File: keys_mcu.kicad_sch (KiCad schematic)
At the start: 26 parts, among them J3 Conn_01x26_Socket, J5 Conn_ARM_JTAG_SWD_10, SW1 PWR, SW2 MUTE, SW2 Volume, SW3 PREV, SW4 PLAY_PAUSE, SW5 NEXT, U2 STM32G431CBUx

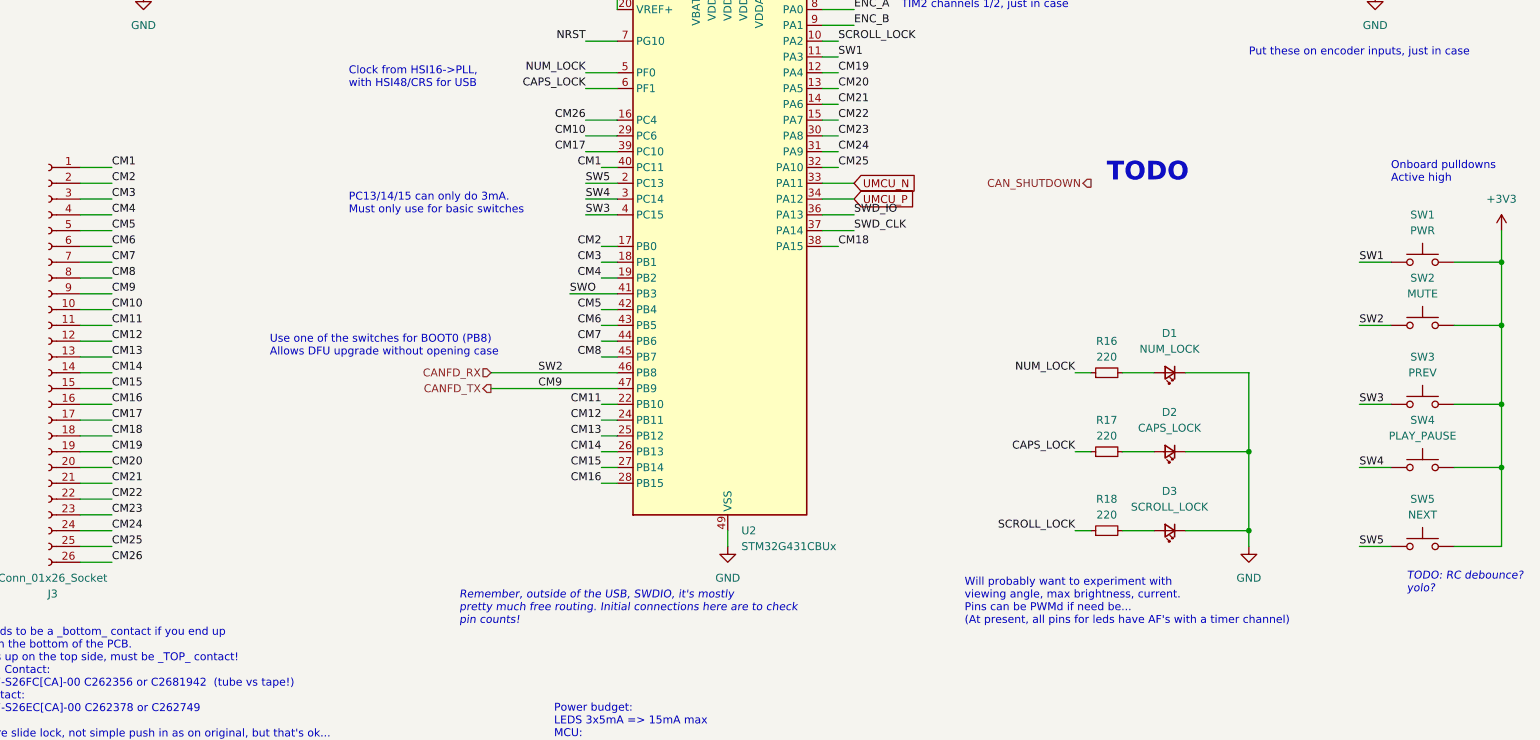
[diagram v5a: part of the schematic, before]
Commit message: unrouted: 0
Juggled all the key matrix IOs and reviewed "all" outstanding TODOs

left: add another cap for downstream Vbus.  it's free, and can only
help.

left: lots of silk?
left: place as much free io to pads as can be easily done, for
test/board reuse.
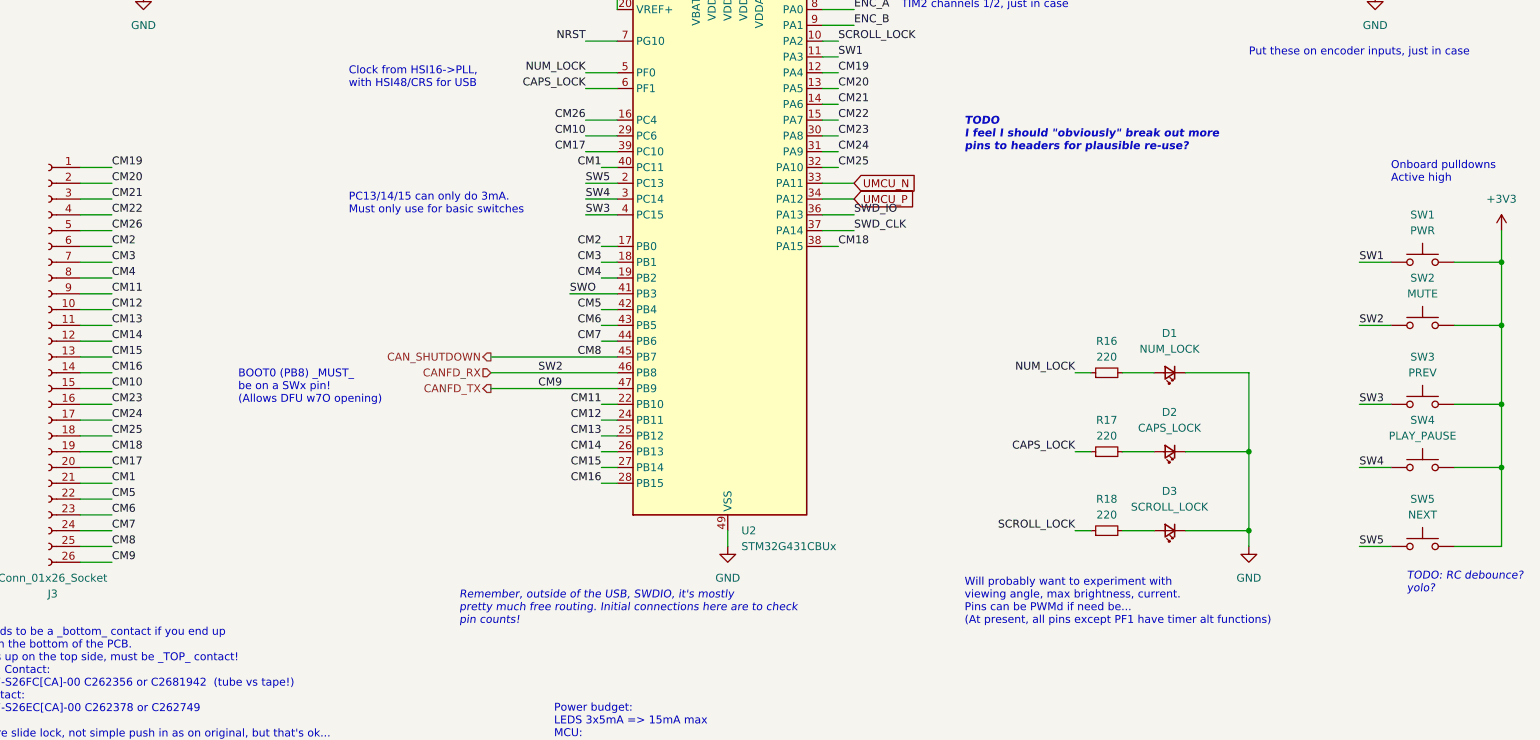
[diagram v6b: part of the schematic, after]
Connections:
- net CANFD_TX: now also J3.26 (Pin_26); no longer J3.9 (Pin_9)
- net CAN_SHUTDOWN: now also J3.25 (Pin_25), U2.45 (PB7)
- net CM1: now also J3.21 (Pin_21); no longer J3.1 (Pin_1)
- net CM10: now also J3.15 (Pin_15); no longer J3.10 (Pin_10)
- net CM11: now also J3.9 (Pin_9); no longer J3.11 (Pin_11)
- net CM12: now also J3.10 (Pin_10); no longer J3.12 (Pin_12)
- net CM13: now also J3.11 (Pin_11); no longer J3.13 (Pin_13)
- net CM14: now also J3.12 (Pin_12); no longer J3.14 (Pin_14)
- net CM15: now also J3.13 (Pin_13); no longer J3.15 (Pin_15)
- net CM16: now also J3.14 (Pin_14); no longer J3.16 (Pin_16)
- net CM17: now also J3.20 (Pin_20); no longer J3.17 (Pin_17)
- net CM18: now also J3.19 (Pin_19); no longer J3.18 (Pin_18)
- net CM19: now also J3.1 (Pin_1); no longer J3.19 (Pin_19)
- net CM2: now also J3.6 (Pin_6); no longer J3.2 (Pin_2)
- net CM20: now also J3.2 (Pin_2); no longer J3.20 (Pin_20)
- net CM21: now also J3.3 (Pin_3); no longer J3.21 (Pin_21)
- net CM22: now also J3.4 (Pin_4); no longer J3.22 (Pin_22)
- net CM23: now also J3.16 (Pin_16); no longer J3.23 (Pin_23)
- net CM24: now also J3.17 (Pin_17); no longer J3.24 (Pin_24)
- net CM25: now also J3.18 (Pin_18); no longer J3.25 (Pin_25)
- net CM26: now also J3.5 (Pin_5); no longer J3.26 (Pin_26)
- net CM3: now also J3.7 (Pin_7); no longer J3.3 (Pin_3)
- net CM4: now also J3.8 (Pin_8); no longer J3.4 (Pin_4)
- net CM5: now also J3.22 (Pin_22); no longer J3.5 (Pin_5)
- net CM6: now also J3.23 (Pin_23); no longer J3.6 (Pin_6)
- net CM7: now also J3.24 (Pin_24); no longer J3.7 (Pin_7)
- removed net CM8: J3.8 (Pin_8), U2.45 (PB7)
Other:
- note added: "BOOT0 (PB8) _MUST_ be on a SWx pin! (Allows DFU w7O opening)"
- note added: "TODO I feel I should "obviously" break out more pins to headers for plausible re-use?"
- note added: "Will probably want to experiment with viewing angle, max brightness, current. Pins can be PWMd if need be... (At present, all pins except PF1 have timer alt functions)"
- note removed: "TODO"
- note removed: "Use one of the switches for BOOT0 (PB8) Allows DFU upgrade without opening case"
- note removed: "Will probably want to experiment with viewing angle, max brightness, current. Pins can be PWMd if need be... (At present, all pins for leds have AF's with a timer channel)"
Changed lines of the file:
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@@
-    (stroke (width 0) (type default))
-  )
-  (wire (pts (xy 121.92 116.84) (xy 124.46 116.84))
     (stroke (width 0) (type default))
   )
@@
   )
   (wire (pts (xy 157.48 33.02) (xy 157.48 35.56))
+    (stroke (width 0) (type default))
+  )
+  (wire (pts (xy 104.14 116.84) (xy 124.46 116.84))
     (stroke (width 0) (type default))
   )
@@
     (effects (font (size 1.27 1.27) italic) (justify left bottom))
   )
-  (text "Use one of the switches for BOOT0 (PB8)\nAllows DFU upgrade without opening case"
-    (at 68.58 116.84 0)
-    (effects (font (size 1.27 1.27)) (justify left bottom))
-  )
-  (text "Will probably want to experiment with\nviewing angle, max brightness, current.\nPins can be PWMd if need be...\n(At present, all pins for leds have AF's with a timer channel)"
+  (text "BOOT0 (PB8) _MUST_\nbe on a SWx pin!\n(Allows DFU w7O opening)"
+    (at 63.5 124.46 0)
+    (effects (font (size 1.27 1.27)) (justify left bottom))
+  )
+  (text "Will probably want to experiment with\nviewing angle, max brightness, current.\nPins can be PWMd if need be...\n(At present, all pins except PF1 have timer alt functions)"
     (at 180.34 160.02 0)
     (effects (font (size 1.27 1.27)) (justify left bottom))
@@
     (at 81.28 93.98 0)
     (effects (font (size 1.27 1.27)) (justify left bottom))
-  )
-  (text "TODO" (at 203.2 88.9 0)
-    (effects (font (size 3 3) (thickness 0.6) bold (color 255 23 46 1)) (justify left bottom))
   )
   (text "Remember, outside of the USB, SWDIO, it's mostly\npretty much free routing. Initial connections here are to check\npin counts!"
@@
     (effects (font (size 1.27 1.27)) (justify left bottom))
   )
+  (text "TODO\nI feel I should \"obviously\" break out more\npins to headers for plausible re-use?"
+    (at 180.34 83.82 0)
+    (effects (font (size 1.27 1.27) bold italic) (justify left bottom))
+  )
   (text "We're not sure about the height of this...." (at 241.3 27.94 0)
     (effects (font (size 1.27 1.27)) (justify left bottom))
   )
-  (label "CM14" (at 43.18 119.38 0) (fields_autoplaced)
+  (label "CM14" (at 43.18 114.3 0) (fields_autoplaced)
     (effects (font (size 1.27 1.27)) (justify left bottom))
   )
@@
     (effects (font (size 1.27 1.27)) (justify left bottom))
   )
-  (label "CM5" (at 43.18 96.52 0) (fields_autoplaced)
+  (label "CM5" (at 43.18 139.7 0) (fields_autoplaced)
     (effects (font (size 1.27 1.27)) (justify left bottom))
   )
@@
     (effects (font (size 1.27 1.27)) (justify right bottom))
   )
-  (label "CM22" (at 43.18 139.7 0) (fields_autoplaced)
-    (effects (font (size 1.27 1.27)) (justify left bottom))
-  )
-  (label "CM15" (at 43.18 121.92 0) (fields_autoplaced)
+  (label "CM22" (at 43.18 93.98 0) (fields_autoplaced)
+    (effects (font (size 1.27 1.27)) (justify left bottom))
+  )
+  (label "CM15" (at 43.18 116.84 0) (fields_autoplaced)
     (effects (font (size 1.27 1.27)) (justify left bottom))
   )
@@
     (effects (font (size 1.27 1.27)) (justify left bottom))
   )
-  (label "CM23" (at 43.18 142.24 0) (fields_autoplaced)
-    (effects (font (size 1.27 1.27)) (justify left bottom))
-  )
-  (label "CM2" (at 43.18 88.9 0) (fields_autoplaced)
-    (effects (font (size 1.27 1.27)) (justify left bottom))
-  )
-  (label "CM1" (at 43.18 86.36 0) (fields_autoplaced)
-    (effects (font (size 1.27 1.27)) (justify left bottom))
-  )
-  (label "CM11" (at 43.18 111.76 0) (fields_autoplaced)
-    (effects (font (size 1.27 1.27)) (justify left bottom))
-  )
-  (label "CM7" (at 43.18 101.6 0) (fields_autoplaced)
+  (label "CM23" (at 43.18 124.46 0) (fields_autoplaced)
+    (effects (font (size 1.27 1.27)) (justify left bottom))
+  )
+  (label "CM2" (at 43.18 99.06 0) (fields_autoplaced)
+    (effects (font (size 1.27 1.27)) (justify left bottom))
+  )
+  (label "CM1" (at 43.18 137.16 0) (fields_autoplaced)
+    (effects (font (size 1.27 1.27)) (justify left bottom))
+  )
+  (label "CM11" (at 43.18 106.68 0) (fields_autoplaced)
+    (effects (font (size 1.27 1.27)) (justify left bottom))
+  )
+  (label "CM7" (at 43.18 144.78 0) (fields_autoplaced)
     (effects (font (size 1.27 1.27)) (justify left bottom))
   )
@@
     (effects (font (size 1.27 1.27)) (justify left bottom))
   )
-  (label "CM4" (at 43.18 93.98 0) (fields_autoplaced)
+  (label "CM4" (at 43.18 104.14 0) (fields_autoplaced)
     (effects (font (size 1.27 1.27)) (justify left bottom))
   )
@@
     (effects (font (size 1.27 1.27)) (justify left bottom))
   )
-  (label "CM12" (at 43.18 114.3 0) (fields_autoplaced)
+  (label "CM12" (at 43.18 109.22 0) (fields_autoplaced)
     (effects (font (size 1.27 1.27)) (justify left bottom))
   )
@@
     (effects (font (size 1.27 1.27)) (justify right bottom))
   )
-  (label "CM10" (at 43.18 109.22 0) (fields_autoplaced)
+  (label "CM10" (at 43.18 121.92 0) (fields_autoplaced)
     (effects (font (size 1.27 1.27)) (justify left bottom))
   )
@@
     (effects (font (size 1.27 1.27)) (justify right bottom))
   )
-  (label "CM26" (at 43.18 149.86 0) (fields_autoplaced)
-    (effects (font (size 1.27 1.27)) (justify left bottom))
-  )
-  (label "CM25" (at 43.18 147.32 0) (fields_autoplaced)
+  (label "CM26" (at 43.18 96.52 0) (fields_autoplaced)
+    (effects (font (size 1.27 1.27)) (justify left bottom))
+  )
+  (label "CM25" (at 43.18 129.54 0) (fields_autoplaced)
     (effects (font (size 1.27 1.27)) (justify left bottom))
   )
@@
     (effects (font (size 1.27 1.27)) (justify left bottom))
   )
-  (label "CM18" (at 43.18 129.54 0) (fields_autoplaced)
+  (label "CM18" (at 43.18 132.08 0) (fields_autoplaced)
     (effects (font (size 1.27 1.27)) (justify left bottom))
   )
@@
     (effects (font (size 1.27 1.27)) (justify left bottom))
   )
-  (label "CM8" (at 43.18 104.14 0) (fields_autoplaced)
+  (label "CM8" (at 43.18 147.32 0) (fields_autoplaced)
     (effects (font (size 1.27 1.27)) (justify left bottom))
   )
@@
     (effects (font (size 1.27 1.27)) (justify right bottom))
   )
-  (label "CM21" (at 43.18 137.16 0) (fields_autoplaced)
+  (label "CM21" (at 43.18 91.44 0) (fields_autoplaced)
     (effects (font (size 1.27 1.27)) (justify left bottom))
   )
@@
     (effects (font (size 1.27 1.27)) (justify left bottom))
   )
-  (label "CM24" (at 43.18 144.78 0) (fields_autoplaced)
-    (effects (font (size 1.27 1.27)) (justify left bottom))
-  )
-  (label "CM19" (at 43.18 132.08 0) (fields_autoplaced)
+  (label "CM24" (at 43.18 127 0) (fields_autoplaced)
+    (effects (font (size 1.27 1.27)) (justify left bottom))
+  )
+  (label "CM19" (at 43.18 86.36 0) (fields_autoplaced)
     (effects (font (size 1.27 1.27)) (justify left bottom))
   )
@@
     (effects (font (size 1.27 1.27)) (justify right bottom))
   )
-  (label "CM9" (at 43.18 106.68 0) (fields_autoplaced)
-    (effects (font (size 1.27 1.27)) (justify left bottom))
-  )
-  (label "CM13" (at 43.18 116.84 0) (fields_autoplaced)
+  (label "CM9" (at 43.18 149.86 0) (fields_autoplaced)
+    (effects (font (size 1.27 1.27)) (justify left bottom))
+  )
+  (label "CM13" (at 43.18 111.76 0) (fields_autoplaced)
     (effects (font (size 1.27 1.27)) (justify left bottom))
   )
@@
     (effects (font (size 1.27 1.27)) (justify left bottom))
   )
-  (label "CM3" (at 43.18 91.44 0) (fields_autoplaced)
-    (effects (font (size 1.27 1.27)) (justify left bottom))
-  )
-  (label "CM16" (at 43.18 124.46 0) (fields_autoplaced)
+  (label "CM3" (at 43.18 101.6 0) (fields_autoplaced)
+    (effects (font (size 1.27 1.27)) (justify left bottom))
+  )
+  (label "CM16" (at 43.18 119.38 0) (fields_autoplaced)
     (effects (font (size 1.27 1.27)) (justify left bottom))
   )
@@
     (effects (font (size 1.27 1.27)) (justify right bottom))
   )
-  (label "CM6" (at 43.18 99.06 0) (fields_autoplaced)
+  (label "CM6" (at 43.18 142.24 0) (fields_autoplaced)
     (effects (font (size 1.27 1.27)) (justify left bottom))
   )
@@
     (effects (font (size 1.27 1.27)) (justify left bottom))
   )
-  (label "CM20" (at 43.18 134.62 0) (fields_autoplaced)
+  (label "CM20" (at 43.18 88.9 0) (fields_autoplaced)
     (effects (font (size 1.27 1.27)) (justify left bottom))
   )
@@
     (effects (font (size 1.27 1.27)) (justify right bottom))
   )
-  (label "CM17" (at 43.18 127 0) (fields_autoplaced)
+  (label "CM17" (at 43.18 134.62 0) (fields_autoplaced)
     (effects (font (size 1.27 1.27)) (justify left bottom))
   )
@@
     (effects (font (size 1.27 1.27)) (justify right))
   )
-  (hierarchical_label "CAN_SHUTDOWN" (shape output) (at 200.66 88.9 180) (fields_autoplaced)
+  (hierarchical_label "CAN_SHUTDOWN" (shape output) (at 104.14 116.84 180) (fields_autoplaced)
     (effects (font (size 1.27 1.27)) (justify right))
   )

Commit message: shuffled, added bonus, silked up...
Nearly there..?
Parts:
- added J6: Conn_01x06_Socket, Connector_PinHeader_2.54mm:PinHeader_1x06_P2.54mm_Vertical, symbol Connector:Conn_01x06_Socket
- added R21: 10k, Resistor_SMD:R_0603_1608Metric, symbol Device:R_Small
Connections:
- net CANFD_RX: now also R21.2
- net CM14: now also J6.1 (Pin_1)
- net CM15: now also J6.2 (Pin_2)
- net CM16: now also J6.3 (Pin_3)
- net CM23: now also J6.4 (Pin_4)
- net CM24: now also J6.5 (Pin_5)
- net CM25: now also J6.6 (Pin_6)
- net GND: now also R21.1
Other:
- note added: "A10 A9 A8 B15 B14 B13"
- note added: "BOOT0 (PB8) _MUST_ be on a SWx pin! (Allows DFU w/O opening)"
- note added: "Extra Bonus Breakout! ;) 1xSPI, 1xUART, 1xi2c on 6 pins PA8 (i2c2-sda), PA9 (i2c2-scl, usart1-tx), PA10 (usart1-rx), PB13 (spi2-sck, usart3-cts), PB14 (spi2-miso, usart3-rts/de), PB15 (spi2-mosi)"
- note added: "Must be _low_ to boot normally. high for DFU and we don't want to interfere with canfd? => If it interferes with CAN, we remove it, and use option bits to override boot0"
- note removed: "BOOT0 (PB8) _MUST_ be on a SWx pin! (Allows DFU w7O opening)"
- note removed: "Remember, outside of the USB, SWDIO, it's mostly pretty much free routing. Initial connections here are to check pin counts!"
- note removed: "TODO I feel I should "obviously" break out more pins to headers for plausible re-use?"

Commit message: fix some erc/drc
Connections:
- net GND: now also J5.9 (GNDDetect)
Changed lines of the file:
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@@
   (junction (at 266.7 111.76) (diameter 0) (color 0 0 0 0)
+  )
+  (junction (at 48.26 55.88) (diameter 0) (color 0 0 0 0)
   )
   (junction (at 134.62 25.4) (diameter 0) (color 0 0 0 0)
@@
     (stroke (width 0) (type default))
   )
+  (wire (pts (xy 45.72 55.88) (xy 48.26 55.88))
+    (stroke (width 0) (type default))
+  )
